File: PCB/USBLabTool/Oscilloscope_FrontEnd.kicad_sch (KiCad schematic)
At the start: 94 parts, among them J1 Chanel 0 input, J10 T_pwm, J12 T_buf, J14 ADC1, J15 ADC2, J16 +3.3VA, J2 Chanel 1 input, J4 T_att, J5 T_acdc, J6 T_acdc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

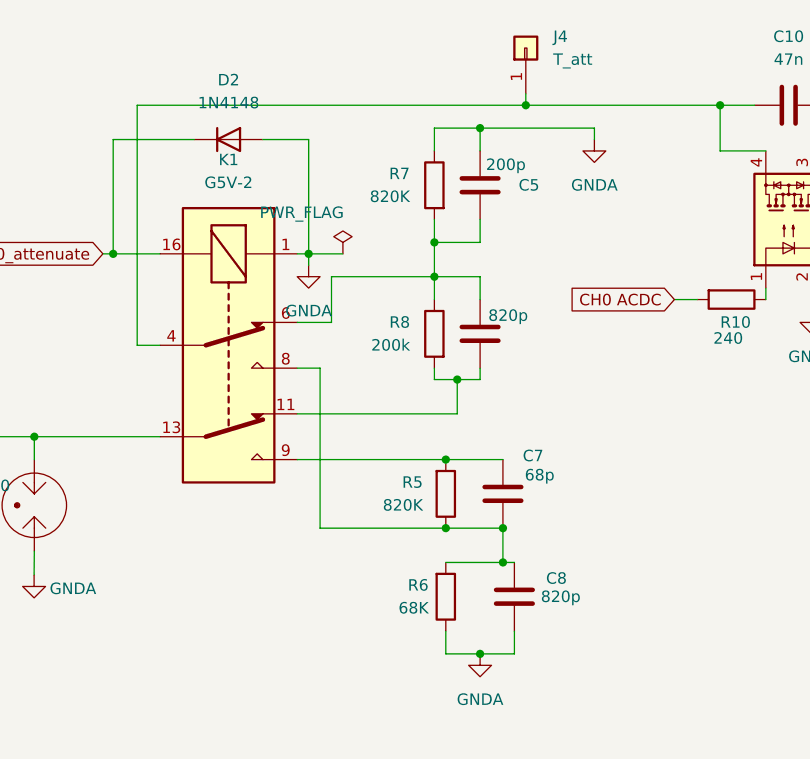
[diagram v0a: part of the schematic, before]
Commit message: update MCU and USB, fix some footprints
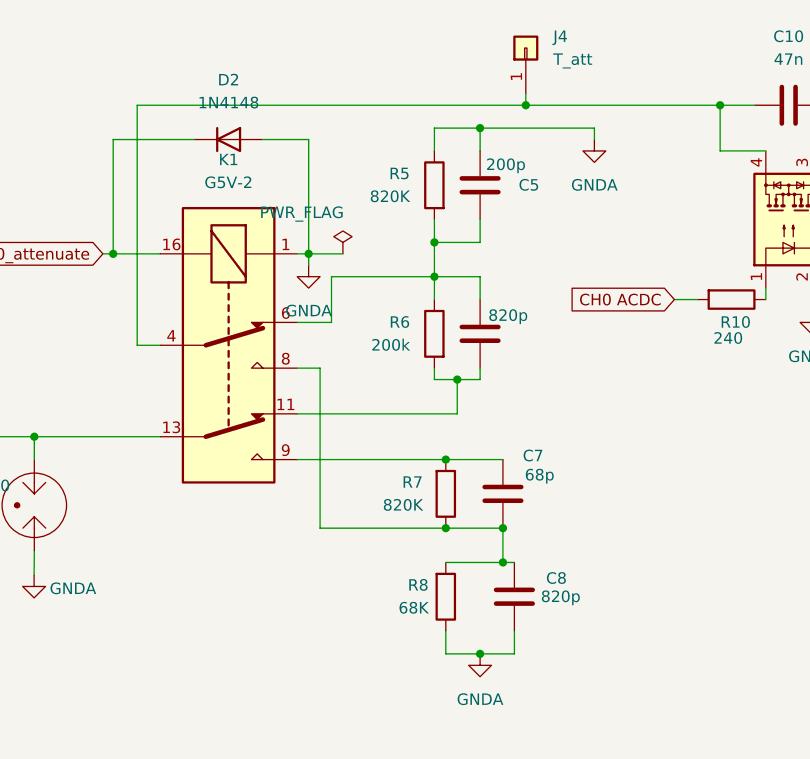
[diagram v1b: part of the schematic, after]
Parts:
- renumbered R7 to R5, R8 to R6, R5 to R7, R6 to R8

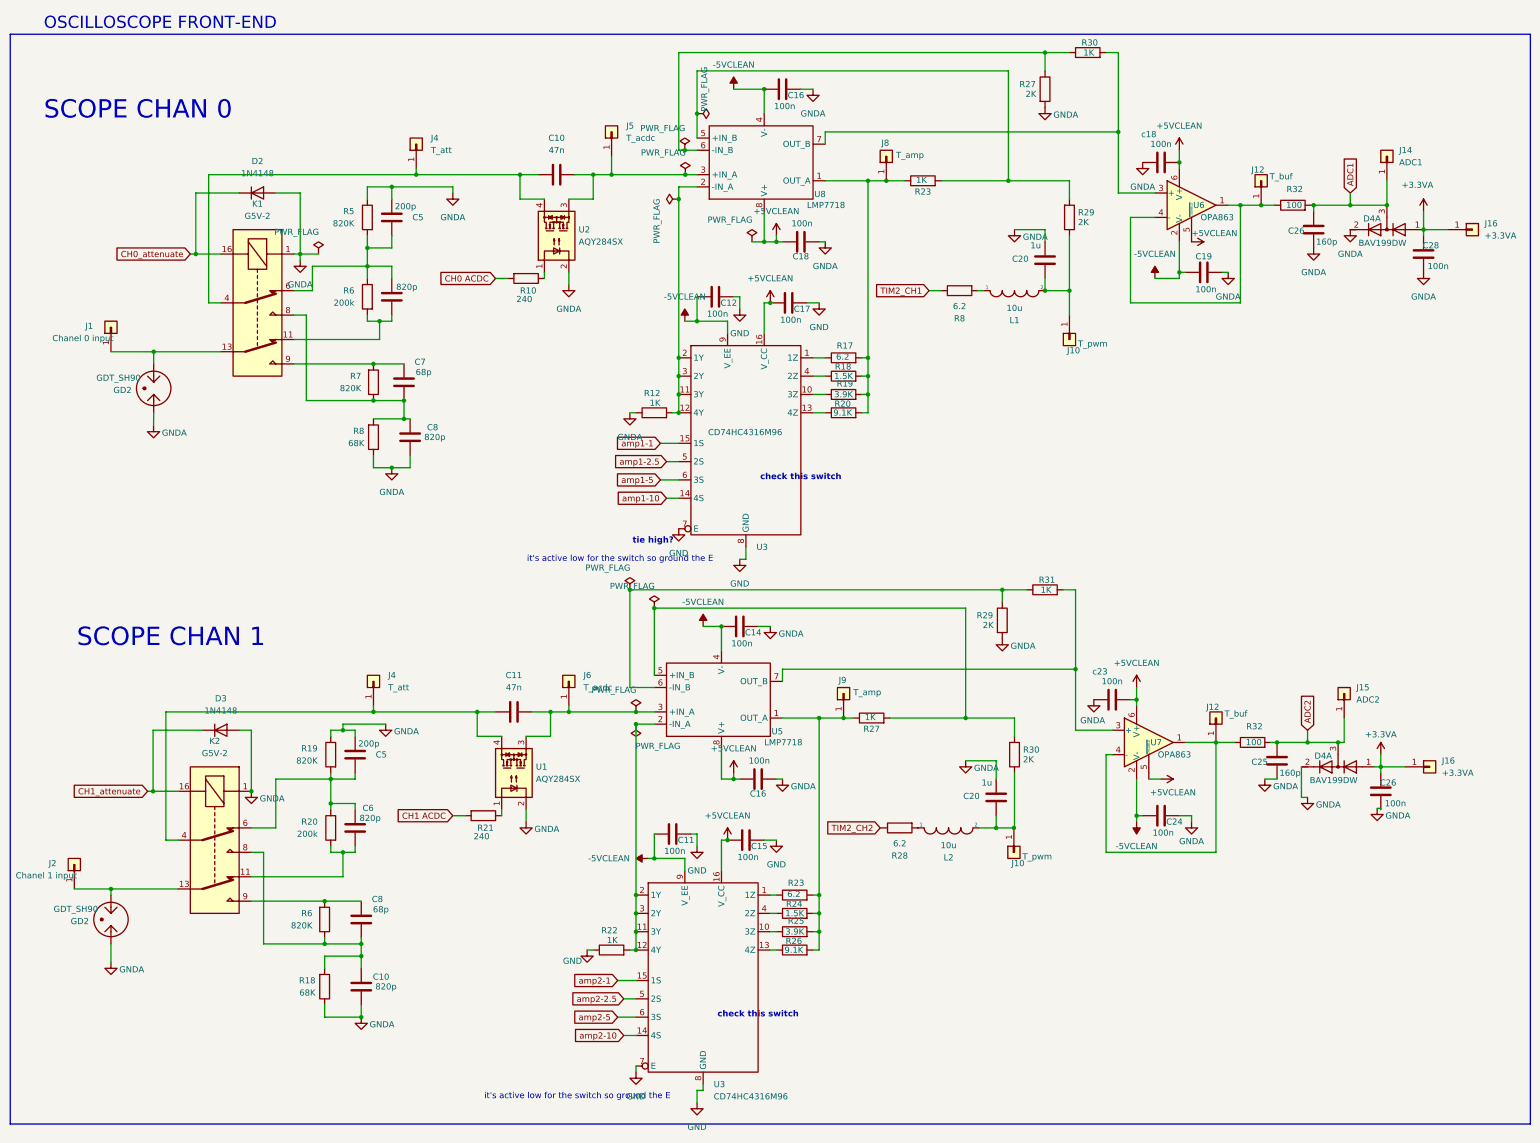
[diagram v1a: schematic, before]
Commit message: modify MCU and name tags
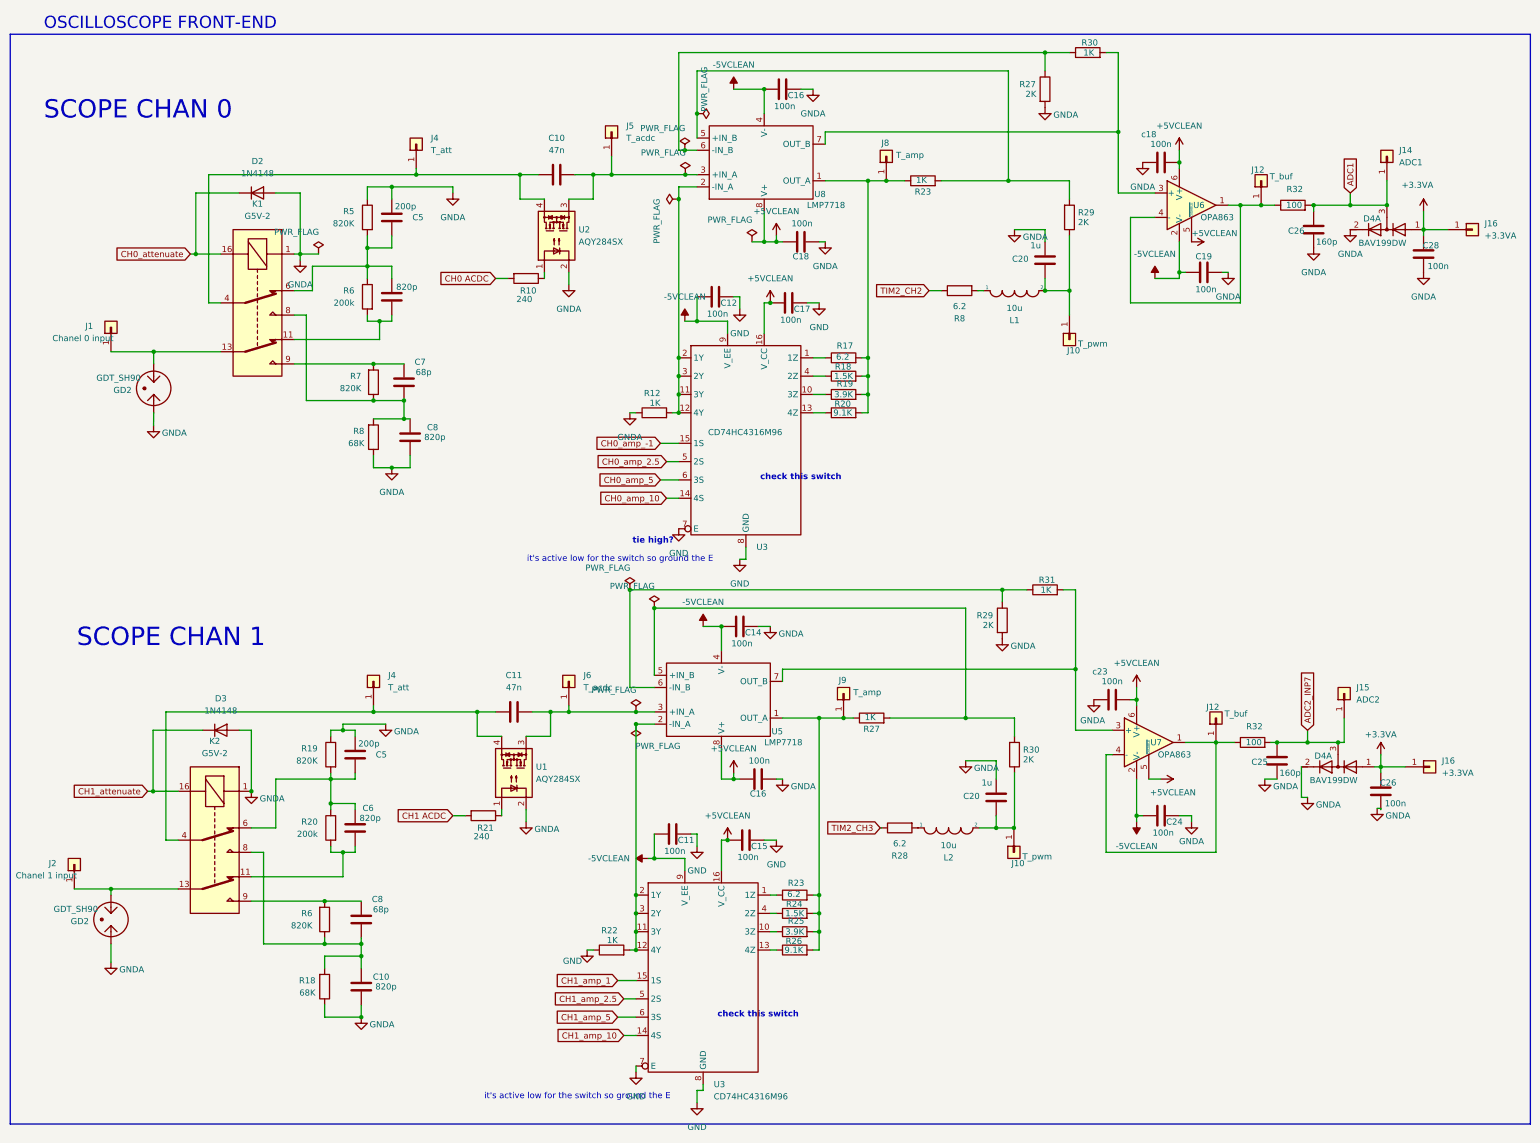
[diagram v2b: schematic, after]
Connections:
- net TIM2_CH1 is gone; now on net TIM2_CH2: R8.1
- net TIM2_CH2: no longer R28.1
- net ADC2 renamed ADC2_INP7
- net amp1-1 renamed CH0_amp_-1
- net amp1-10 renamed CH0_amp_10
- net amp1-2.5 renamed CH0_amp_2.5
- net amp1-5 renamed CH0_amp_5
- net amp2-1 renamed CH1_amp_1
- net amp2-10 renamed CH1_amp_10
- net amp2-2.5 renamed CH1_amp_2.5
- net amp2-5 renamed CH1_amp_5
- new net TIM2_CH3: R28.1
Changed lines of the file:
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@@
 		)
 	)
-	(global_label "amp2-1"
+	(global_label "CH1_amp_1"
 		(shape input)
 		(at 144.78 219.71 180)
@@
 		)
 		(property "Intersheetrefs" "${INTERSHEET_REFS}"
-			(at 133.8121 219.71 0)
+			(at 130.8488 219.71 0)
 			(effects
 				(font
@@
 		)
 	)
-	(global_label "amp1-2.5"
+	(global_label "CH0_amp_2.5"
 		(shape input)
 		(at 154.94 111.76 180)
@@
 		)
 		(property "Intersheetrefs" "${INTERSHEET_REFS}"
-			(at 142.7298 111.6806 0)
-			(effects
-				(font
-					(size 1.27 1.27)
-				)
-				(justify right)
-				(hide yes)
-			)
-		)
-	)
-	(global_label "amp2-5"
+			(at 139.1945 111.76 0)
+			(effects
+				(font
+					(size 1.27 1.27)
+				)
+				(justify right)
+				(hide yes)
+			)
+		)
+	)
+	(global_label "CH1_amp_5"
 		(shape input)
 		(at 144.78 227.33 180)
@@
 		)
 		(property "Intersheetrefs" "${INTERSHEET_REFS}"
-			(at 133.8121 227.33 0)
-			(effects
-				(font
-					(size 1.27 1.27)
-				)
-				(justify right)
-				(hide yes)
-			)
-		)
-	)
-	(global_label "amp2-10"
+			(at 130.8488 227.33 0)
+			(effects
+				(font
+					(size 1.27 1.27)
+				)
+				(justify right)
+				(hide yes)
+			)
+		)
+	)
+	(global_label "CH1_amp_10"
 		(shape input)
 		(at 146.05 231.14 180)
@@
 		)
 		(property "Intersheetrefs" "${INTERSHEET_REFS}"
-			(at 133.8726 231.14 0)
-			(effects
-				(font
-					(size 1.27 1.27)
-				)
-				(justify right)
-				(hide yes)
-			)
-		)
-	)
-	(global_label "amp2-2.5"
+			(at 130.9093 231.14 0)
+			(effects
+				(font
+					(size 1.27 1.27)
+				)
+				(justify right)
+				(hide yes)
+			)
+		)
+	)
+	(global_label "CH1_amp_2.5"
 		(shape input)
 		(at 146.05 223.52 180)
@@
 		)
 		(property "Intersheetrefs" "${INTERSHEET_REFS}"
-			(at 133.2678 223.52 0)
+			(at 130.3045 223.52 0)
 			(effects
 				(font
@@
 		)
 	)
-	(global_label "amp1-1"
+	(global_label "CH0_amp_-1"
 		(shape input)
 		(at 153.67 107.95 180)
@@
 		)
 		(property "Intersheetrefs" "${INTERSHEET_REFS}"
-			(at 143.274 107.8706 0)
-			(effects
-				(font
-					(size 1.27 1.27)
-				)
-				(justify right)
-				(hide yes)
-			)
-		)
-	)
-	(global_label "amp1-5"
+			(at 138.1664 107.95 0)
+			(effects
+				(font
+					(size 1.27 1.27)
+				)
+				(justify right)
+				(hide yes)
+			)
+		)
+	)
+	(global_label "CH0_amp_5"
 		(shape input)
 		(at 153.67 115.57 180)
@@
 		)
 		(property "Intersheetrefs" "${INTERSHEET_REFS}"
-			(at 143.274 115.4906 0)
-			(effects
-				(font
-					(size 1.27 1.27)
-				)
-				(justify right)
-				(hide yes)
-			)
-		)
-	)
-	(global_label "TIM2_CH1"
+			(at 139.7388 115.57 0)
+			(effects
+				(font
+					(size 1.27 1.27)
+				)
+				(justify right)
+				(hide yes)
+			)
+		)
+	)
+	(global_label "TIM2_CH2"
 		(shape input)
 		(at 209.55 76.2 180)
@@
 		)
 	)
-	(global_label "amp1-10"
+	(global_label "CH0_amp_10"
 		(shape input)
 		(at 154.94 119.38 180)
@@
 		)
 		(property "Intersheetrefs" "${INTERSHEET_REFS}"
-			(at 143.3345 119.3006 0)
-			(effects
-				(font
-					(size 1.27 1.27)
-				)
-				(justify right)
-				(hide yes)
-			)
-		)
-	)
-	(global_label "ADC2"
+			(at 139.7993 119.38 0)
+			(effects
+				(font
+					(size 1.27 1.27)
+				)
+				(justify right)
+				(hide yes)
+			)
+		)
+	)
+	(global_label "ADC2_INP7"
 		(shape input)
 		(at 288.29 167.64 90)
@@
 		)
 		(property "Intersheetrefs" "${INTERSHEET_REFS}"
-			(at 288.29 159.8167 90)
+			(at 288.29 154.4343 90)
 			(effects
 				(font
@@
 		)
 	)
-	(global_label "TIM2_CH2"
+	(global_label "TIM2_CH3"
 		(shape input)
 		(at 199.39 187.96 180)

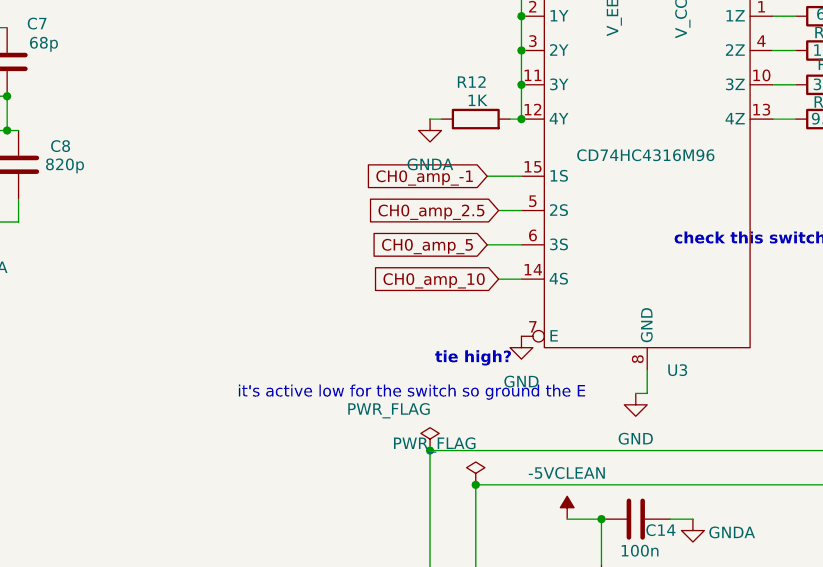
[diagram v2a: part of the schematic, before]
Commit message: Fixed up footprints
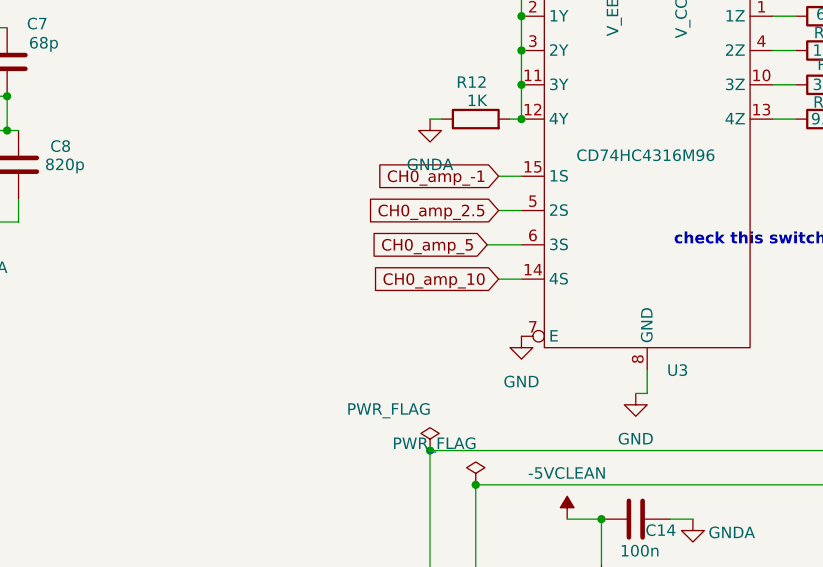
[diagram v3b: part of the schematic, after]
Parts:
- GD2: footprint footprints:GDT_SH_LTF -> userfp:GDT_SH_LTF
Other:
- note removed: "tie high?"
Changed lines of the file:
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@@
 	(wire
 		(pts
-			(xy 153.67 107.95) (xy 157.48 107.95)
+			(xy 154.94 107.95) (xy 157.48 107.95)
 		)
 		(stroke
@@
 		)
 	)
-	(text "it's active low for the switch so ground the E\n"
-		(exclude_from_sim no)
-		(at 145.288 132.08 0)
-		(effects
-			(font
-				(size 1.27 1.27)
-			)
-		)
-	)
 	(text "SCOPE CHAN 0\n"
 		(exclude_from_sim no)
@@
 		)
 	)
-	(text "tie high?"
-		(exclude_from_sim no)
-		(at 152.146 128.27 0)
-		(effects
-			(font
-				(size 1.27 1.27)
-				(thickness 0.254)
-				(bold yes)
-			)
-		)
-	)
 	(text "check this switch"
 		(exclude_from_sim no)
@@
 	(global_label "CH0_amp_-1"
 		(shape input)
-		(at 153.67 107.95 180)
+		(at 154.94 107.95 180)
 		(fields_autoplaced yes)
 		(effects
@@
 		)
 		(property "Intersheetrefs" "${INTERSHEET_REFS}"
-			(at 138.1664 107.95 0)
+			(at 139.4364 107.95 0)
 			(effects
 				(font
@@
 			)
 		)
-		(property "Footprint" "footprints:GDT_SH_LTF"
+		(property "Footprint" "userfp:GDT_SH_LTF"
 			(at 54.356 96.774 90)
 			(effects
@@
 			)
 		)
-		(property "Footprint" "footprints:GDT_SH_LTF"
+		(property "Footprint" "userfp:GDT_SH_LTF"
 			(at 45.466 207.264 90)
 			(effects

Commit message: Started adding 20pin
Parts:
- removed J1: Chanel 0 input, Connector_PinHeader_2.54mm:PinHeader_1x01_P2.54mm_Vertical, symbol Connector_Generic:Conn_01x01
- removed J2: Chanel 1 input, Connector_PinHeader_2.54mm:PinHeader_1x01_P2.54mm_Vertical, symbol Connector_Generic:Conn_01x01
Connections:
- net P_CH0_IN: now reaches GD2.1, K1.13
- net P_CH1_IN: now reaches GD2.1, K2.13
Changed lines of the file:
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@@
 		)
 	)
+	(global_label "P_CH0_IN"
+		(shape input)
+		(at 39.37 88.9 180)
+		(fields_autoplaced yes)
+		(effects
+			(font
+				(size 1.27 1.27)
+			)
+			(justify right)
+		)
+		(property "Intersheetrefs" "${INTERSHEET_REFS}"
+			(at 27.4343 88.9 0)
+			(effects
+				(font
+					(size 1.27 1.27)
+				)
+				(justify right)
+				(hide yes)
+			)
+		)
+	)
 	(global_label "CH1_attenuate"
 		(shape input)
@@
 		)
 	)
+	(global_label "P_CH1_IN"
+		(shape input)
+		(at 31.75 200.66 180)
+		(fields_autoplaced yes)
+		(effects
+			(font
+				(size 1.27 1.27)
+			)
+			(justify right)
+		)
+		(property "Intersheetrefs" "${INTERSHEET_REFS}"
+			(at 19.8143 200.66 0)
+			(effects
+				(font
+					(size 1.27 1.27)
+				)
+				(justify right)
+				(hide yes)
+			)
+		)
+	)
 	(global_label "TIM2_CH3"
 		(shape input)
@@
 	)
 	(symbol
-		(lib_id "Connector_Generic:Conn_01x01")
-		(at 39.37 83.82 90)
-		(unit 1)
-		(exclude_from_sim no)
-		(in_bom yes)
-		(on_board yes)
-		(dnp no)
-		(property "Reference" "J1"
-			(at 34.036 83.566 90)
-			(effects
-				(font
-					(size 1.27 1.27)
-				)
-				(justify right)
-			)
-		)
-		(property "Value" "Chanel 0 input"
-			(at 27.178 86.106 90)
-			(effects
-				(font
-					(size 1.27 1.27)
-				)
-				(justify right)
-			)
-		)
-		(property "Footprint" "Connector_PinHeader_2.54mm:PinHeader_1x01_P2.54mm_Vertical"
-			(at 39.37 83.82 0)
-			(effects
-				(font
-					(size 1.27 1.27)
-				)
-				(hide yes)
-			)
-		)
-		(property "Datasheet" "~"
-			(at 39.37 83.82 0)
-			(effects
-				(font
-					(size 1.27 1.27)
-				)
-				(hide yes)
-			)
-		)
-		(property "Description" ""
-			(at 39.37 83.82 0)
-			(effects
-				(font
-					(size 1.27 1.27)
-				)
-				(hide yes)
-			)
-		)
-		(pin "1"
-		)
-		(instances
-			(project "Oscilloscope_FrontEnd"
-				(path "/8154ece5-3057-47b0-ace6-3a152b9b167f"
-					(reference "J1")
-					(unit 1)
-				)
-			)
-			(project ""
-				(path "/b5440f7d-90d5-417e-adc2-aa6b11e5424d/4269701b-4537-45be-98a2-a1633b405066"
-					(reference "J2")
-					(unit 1)
-				)
-			)
-		)
-	)
-	(symbol
 		(lib_id "Device:R")
 		(at 191.77 97.79 90)
@@
 					(unit 1)
 				)
-			)
-		)
-	)
-	(symbol
-		(lib_id "Connector_Generic:Conn_01x01")
-		(at 31.75 195.58 90)
-		(unit 1)
-		(exclude_from_sim no)
-		(in_bom yes)
-		(on_board yes)
-		(dnp no)
-		(property "Reference" "J2"
-			(at 26.416 195.326 90)
-			(effects
-				(font
-					(size 1.27 1.27)
-				)
-				(justify right)
-			)
-		)
-		(property "Value" "Chanel 1 input"
-			(at 19.558 197.866 90)
-			(effects
-				(font
-					(size 1.27 1.27)
-				)
-				(justify right)
-			)
-		)
-		(property "Footprint" "Connector_PinHeader_2.54mm:PinHeader_1x01_P2.54mm_Vertical"
-			(at 31.75 195.58 0)
-			(effects
-				(font
-					(size 1.27 1.27)
-				)
-				(hide yes)
-			)
-		)
-		(property "Datasheet" "~"
-			(at 31.75 195.58 0)
-			(effects
-				(font
-					(size 1.27 1.27)
-				)
-				(hide yes)
-			)
-		)
-		(property "Description" ""
-			(at 31.75 195.58 0)
-			(effects
-				(font
-					(size 1.27 1.27)
-				)
-				(hide yes)
-			)
-		)
-		(pin "1"
-		)
-		(instances
-			(project "Oscilloscope_FrontEnd"
-				(path "/8154ece5-3057-47b0-ace6-3a152b9b167f"
-					(reference "J2")
-					(unit 1)
-				)
-			)
-			(project ""
-				(path "/b5440f7d-90d5-417e-adc2-aa6b11e5424d/4269701b-4537-45be-98a2-a1633b405066"
-					(reference "J1")
-					(unit 1)
-				)

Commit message: minor fixes
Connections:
- net CH0_amp_-1 renamed CH0_amp_1
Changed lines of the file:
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@@
 		)
 	)
-	(global_label "CH0_amp_-1"
+	(global_label "CH0_amp_1"
 		(shape input)
 		(at 154.94 107.95 180)
@@
 		)
 		(property "Intersheetrefs" "${INTERSHEET_REFS}"
-			(at 139.4364 107.95 0)
+			(at 141.0088 107.95 0)
 			(effects
 				(font
